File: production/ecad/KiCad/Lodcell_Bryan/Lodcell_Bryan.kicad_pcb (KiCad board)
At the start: 4 copper layers, 50.7 x 23.5 mm, 24 parts, among them J1 LoadCellConnector, J2 power_for_Loadcell, J3 ConnToESP32, U3 ADS1231IDR, U4 TXB0104DR

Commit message: Renamed designators
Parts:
- moved H1 19.6 mm to (170.4, 41.6)
- moved H4 1.21 mm to (190.5, 41.8)
- renumbered C7 to C2, C2 to C3, C3 to C4, C4 to C5, C5 to C6, C6 to C7, R3 to R1, R1 to R3, U3 to U1, U4 to U2
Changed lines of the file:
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@@
 	(net 1 "SPEED")
 	(net 2 "GND")
-	(net 3 "Net-(U3-CAP1)")
-	(net 4 "Net-(U3-CAP2)")
+	(net 3 "Net-(U1-CAP1)")
+	(net 4 "Net-(U1-CAP2)")
 	(net 5 "+5V")
 	(net 6 "+3.3V")
@@
 	(net 13 "/LP_+")
 	(net 14 "/LP_-")
-	(net 15 "Net-(U4-OE)")
-	(net 16 "Net-(U3-~{DRDY}{slash}DOUT)")
-	(net 17 "Net-(U3-~{PDWN})")
-	(net 18 "Net-(U3-SCLK)")
-	(net 19 "Net-(U3-SPEED)")
+	(net 15 "Net-(U2-OE)")
+	(net 16 "Net-(U1-~{DRDY}{slash}DOUT)")
+	(net 17 "Net-(U1-~{PDWN})")
+	(net 18 "Net-(U1-SCLK)")
+	(net 19 "Net-(U1-SPEED)")
 	(footprint "TXB0104DR:SOIC127P600X175-14N"
 		(layer "F.Cu")
 		(at 185.725 64.94)
-		(property "Reference" "U4"
+		(property "Reference" "U2"
 			(at -4.675 -3.19 180)
 			(layer "F.SilkS")
@@
 			(layers "F.Cu" "F.Paste" "F.Mask")
 			(roundrect_rratio 0.25)
-			(net 16 "Net-(U3-~{DRDY}{slash}DOUT)")
+			(net 16 "Net-(U1-~{DRDY}{slash}DOUT)")
 			(pinfunction "A1")
 			(pintype "input")
@@
 			(layers "F.Cu" "F.Paste" "F.Mask")
 			(roundrect_rratio 0.25)
-			(net 18 "Net-(U3-SCLK)")
+			(net 18 "Net-(U1-SCLK)")
 			(pinfunction "A2")
 			(pintype "input")
@@
 			(layers "F.Cu" "F.Paste" "F.Mask")
 			(roundrect_rratio 0.25)
-			(net 17 "Net-(U3-~{PDWN})")
+			(net 17 "Net-(U1-~{PDWN})")
 			(pinfunction "A3")
 			(pintype "input")
@@
 			(layers "F.Cu" "F.Paste" "F.Mask")
 			(roundrect_rratio 0.25)
-			(net 19 "Net-(U3-SPEED)")
+			(net 19 "Net-(U1-SPEED)")
 			(pinfunction "A4")
 			(pintype "input")
@@
 			(layers "F.Cu" "F.Paste" "F.Mask")
 			(roundrect_rratio 0.25)
-			(net 15 "Net-(U4-OE)")
+			(net 15 "Net-(U2-OE)")
 			(pinfunction "OE")
 			(pintype "input")
@@
 		(descr "Resistor SMD 0805 (2012 Metric), square (rectangular) end terminal, IPC_7351 nominal with elongated pad for handsoldering. (Body size source: IPC-SM-782 page 72, https://www.pcb-3d.com/wordpress/wp-content/uploads/ipc-sm-782a_amendment_1_and_2.pdf), generated with kicad-footprint-generator")
 		(tags "resistor handsolder")
-		(property "Reference" "R3"
+		(property "Reference" "R1"
 			(at 2.5716 0.5034 180)
 			(layer "F.SilkS")
@@
 			(size 1.5 1.5)
 			(layers "F.Cu" "F.Mask")
-			(net 16 "Net-(U3-~{DRDY}{slash}DOUT)")
+			(net 16 "Net-(U1-~{DRDY}{slash}DOUT)")
 			(pinfunction "1")
 			(pintype "passive")
@@
 	(footprint "MountingHole:MountingHole_2.5mm"
 		(layer "F.Cu")
-		(at 190.75 40.575)
+		(at 190.475 41.75)
 		(descr "Mounting Hole 2.5mm, no annular")
 		(tags "mounting hole 2.5mm no annular")
@@
 			(layers "F.Cu" "F.Paste" "F.Mask")
 			(roundrect_rratio 0.208333)
-			(net 15 "Net-(U4-OE)")
+			(net 15 "Net-(U2-OE)")
 			(pintype "passive")
 		)
@@
 		(descr "Capacitor SMD 0805 (2012 Metric), square (rectangular) end terminal, IPC_7351 nominal with elongated pad for handsoldering. (Body size source: IPC-SM-782 page 76, https://www.pcb-3d.com/wordpress/wp-content/uploads/ipc-sm-782a_amendment_1_and_2.pdf, https://docs.google.com/spreadsheets/d/1BsfQQcO9C6DZCsRaXUlFlo91Tg2WpOkGARC1WS5S8t0/edit?usp=sharing), generated with kicad-footprint-generator")
 		(tags "capacitor handsolder")
-		(property "Reference" "C2"
+		(property "Reference" "C3"
 			(at -2.5 0.3 180)
 			(layer "F.SilkS")
@@
 			(layers "F.Cu" "F.Paste" "F.Mask")
 			(roundrect_rratio 0.212766)
-			(net 3 "Net-(U3-CAP1)")
+			(net 3 "Net-(U1-CAP1)")
 			(pintype "passive")
 		)
@@
 			(layers "F.Cu" "F.Paste" "F.Mask")
 			(roundrect_rratio 0.212766)
-			(net 4 "Net-(U3-CAP2)")
+			(net 4 "Net-(U1-CAP2)")
 			(pintype "passive")
 		)
@@
 	(footprint "MountingHole:MountingHole_2.5mm"
 		(layer "F.Cu")
-		(at 151.2 38.125)
+		(at 170.45 41.575)
 		(descr "Mounting Hole 2.5mm, no annular")
 		(tags "mounting hole 2.5mm no annular")
@@
 		(descr "Capacitor SMD 0805 (2012 Metric), square (rectangular) end terminal, IPC_7351 nominal with elongated pad for handsoldering. (Body size source: IPC-SM-782 page 76, https://www.pcb-3d.com/wordpress/wp-content/uploads/ipc-sm-782a_amendment_1_and_2.pdf, https://docs.google.com/spreadsheets/d/1BsfQQcO9C6DZCsRaXUlFlo91Tg2WpOkGARC1WS5S8t0/edit?usp=sharing), generated with kicad-footprint-generator")
 		(tags "capacitor handsolder")
-		(property "Reference" "C5"
+		(property "Reference" "C6"
 			(at -2.5 0.25 180)
 			(layer "F.SilkS")
@@
 		(descr "Capacitor SMD 0805 (2012 Metric), square (rectangular) end terminal, IPC_7351 nominal with elongated pad for handsoldering. (Body size source: IPC-SM-782 page 76, https://www.pcb-3d.com/wordpress/wp-content/uploads/ipc-sm-782a_amendment_1_and_2.pdf, https://docs.google.com/spreadsheets/d/1BsfQQcO9C6DZCsRaXUlFlo91Tg2WpOkGARC1WS5S8t0/edit?usp=sharing), generated with kicad-footprint-generator")
 		(tags "capacitor handsolder")
-		(property "Reference" "C6"
+		(property "Reference" "C7"
 			(at -2.45 0.1 0)
 			(layer "F.SilkS")
@@
 		(descr "Resistor SMD 0805 (2012 Metric), square (rectangular) end terminal, IPC_7351 nominal with elongated pad for handsoldering. (Body size source: IPC-SM-782 page 72, https://www.pcb-3d.com/wordpress/wp-content/uploads/ipc-sm-782a_amendment_1_and_2.pdf), generated with kicad-footprint-generator")
 		(tags "resistor handsolder")
-		(property "Reference" "R1"
+		(property "Reference" "R3"
 			(at 2.5466 0.4784 180)
 			(layer "F.SilkS")
@@
 		(descr "Capacitor SMD 0805 (2012 Metric), square (rectangular) end terminal, IPC_7351 nominal with elongated pad for handsoldering. (Body size source: IPC-SM-782 page 76, https://www.pcb-3d.com/wordpress/wp-content/uploads/ipc-sm-782a_amendment_1_and_2.pdf, https://docs.google.com/spreadsheets/d/1BsfQQcO9C6DZCsRaXUlFlo91Tg2WpOkGARC1WS5S8t0/edit?usp=sharing), generated with kicad-footprint-generator")
 		(tags "capacitor handsolder")
-		(property "Reference" "C3"
+		(property "Reference" "C4"
 			(at 1.05 1.7 180)
 			(layer "F.SilkS")
@@
 		(layer "F.Cu")
 		(at 171.8 66.9)
-		(property "Reference" "U3"
+		(property "Reference" "U1"
 			(at -4.75 -4 0)
 			(layer "F.SilkS")
@@
 			(layers "F.Cu" "F.Paste" "F.Mask")
 			(roundrect_rratio 0.125)
-			(net 19 "Net-(U3-SPEED)")
+			(net 19 "Net-(U1-SPEED)")
 			(pinfunction "SPEED")
 			(pintype "input")
@@
 			(layers "F.Cu" "F.Paste" "F.Mask")
 			(roundrect_rratio 0.125)
-			(net 3 "Net-(U3-CAP1)")
+			(net 3 "Net-(U1-CAP1)")
 			(pinfunction "CAP1")
 			(pintype "passive")
@@
 			(layers "F.Cu" "F.Paste" "F.Mask")
 			(roundrect_rratio 0.125)
-			(net 4 "Net-(U3-CAP2)")
+			(net 4 "Net-(U1-CAP2)")
 			(pinfunction "CAP2")
 			(pintype "passive")
@@
 			(layers "F.Cu" "F.Paste" "F.Mask")
 			(roundrect_rratio 0.125)
-			(net 17 "Net-(U3-~{PDWN})")
+			(net 17 "Net-(U1-~{PDWN})")
 			(pinfunction "~{PDWN}")
 			(pintype "input")
@@
 			(layers "F.Cu" "F.Paste" "F.Mask")
 			(roundrect_rratio 0.125)
-			(net 18 "Net-(U3-SCLK)")
+			(net 18 "Net-(U1-SCLK)")
 			(pinfunction "SCLK")
 			(pintype "input")
@@
 			(layers "F.Cu" "F.Paste" "F.Mask")
 			(roundrect_rratio 0.125)
-			(net 16 "Net-(U3-~{DRDY}{slash}DOUT)")
+			(net 16 "Net-(U1-~{DRDY}{slash}DOUT)")
 			(pinfunction "~{DRDY}/DOUT")
 			(pintype "output")
@@
 			(layers "F.Cu" "F.Paste" "F.Mask")
 			(roundrect_rratio 0.208333)
-			(net 15 "Net-(U4-OE)")
+			(net 15 "Net-(U2-OE)")
 			(pintype "passive")
 		)
@@
 		(descr "Capacitor SMD 0805 (2012 Metric), square (rectangular) end terminal, IPC_7351 nominal with elongated pad for handsoldering. (Body size source: IPC-SM-782 page 76, https://www.pcb-3d.com/wordpress/wp-content/uploads/ipc-sm-782a_amendment_1_and_2.pdf, https://docs.google.com/spreadsheets/d/1BsfQQcO9C6DZCsRaXUlFlo91Tg2WpOkGARC1WS5S8t0/edit?usp=sharing), generated with kicad-footprint-generator")
 		(tags "capacitor handsolder")
-		(property "Reference" "C7"
+		(property "Reference" "C2"
 			(at -0.9909 -1.6466 0)
 			(layer "F.SilkS")
@@
 		(descr "Capacitor SMD 0805 (2012 Metric), square (rectangular) end terminal, IPC_7351 nominal with elongated pad for handsoldering. (Body size source: IPC-SM-782 page 76, https://www.pcb-3d.com/wordpress/wp-content/uploads/ipc-sm-782a_amendment_1_and_2.pdf, https://docs.google.com/spreadsheets/d/1BsfQQcO9C6DZCsRaXUlFlo91Tg2WpOkGARC1WS5S8t0/edit?usp=sharing), generated with kicad-footprint-generator")
 		(tags "capacitor handsolder")
-		(property "Reference" "C4"
+		(property "Reference" "C5"
 			(at -2.55 -0.05 0)
 			(layer "F.SilkS")
@@
 	)
 	(segment
-		(start 164.1466 69.3966)
-		(end 165.225 70.475)
-		(width 0.2)
-		(layer "F.Cu")
-		(net 13)
-	)
-	(segment
-		(start 165.225 70.475)
-		(end 166.2 70.475)
+		(start 164.1466 62.1716)
+		(end 164.1466 69.1216)
 		(width 0.2)
 		(layer "F.Cu")
@@
 	)
 	(segment
-		(start 164.1466 62.1716)
-		(end 164.1466 69.3966)
+		(start 162.8534 60.8784)
+		(end 164.1466 62.1716)
 		(width 0.2)
 		(layer "F.Cu")
@@
 	)
 	(segment
-		(start 162.8534 60.8784)
-		(end 164.1466 62.1716)
+		(start 158.2216 60.8784)
+		(end 162.8534 60.8784)
 		(width 0.2)
 		(layer "F.Cu")
@@
 	)
 	(segment
-		(start 158.2216 60.8784)
-		(end 162.8534 60.8784)
+		(start 164.1466 69.1216)
+		(end 165.5 70.475)
 		(width 0.2)
 		(layer "F.Cu")
@@
 		(width 0.2)
 		(layer "F.Cu")
+		(net 13)
+	)
+	(segment
+		(start 165.5 70.475)
+		(end 166.2 70.475)
+		(width 0.2)
+		(layer "F.Cu")

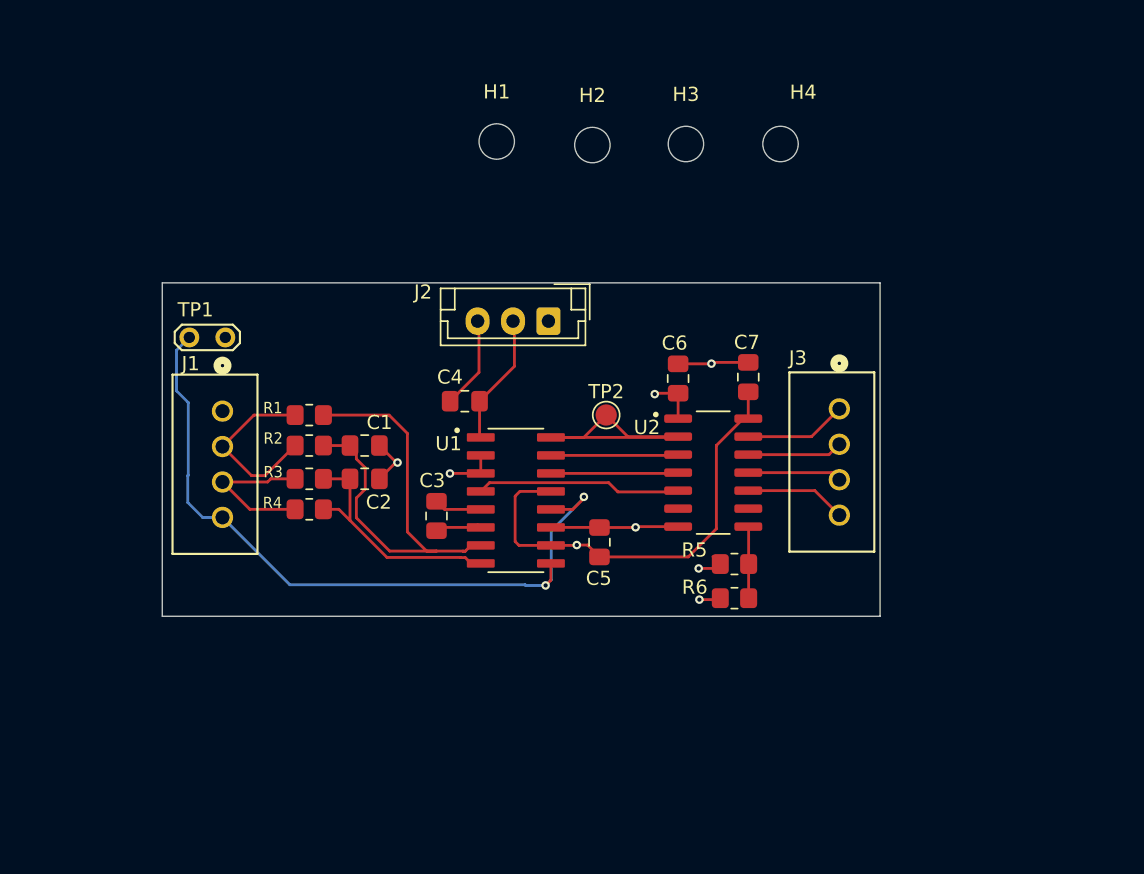
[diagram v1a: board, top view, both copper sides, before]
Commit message: Improved differential signals. switched to 2 layer board
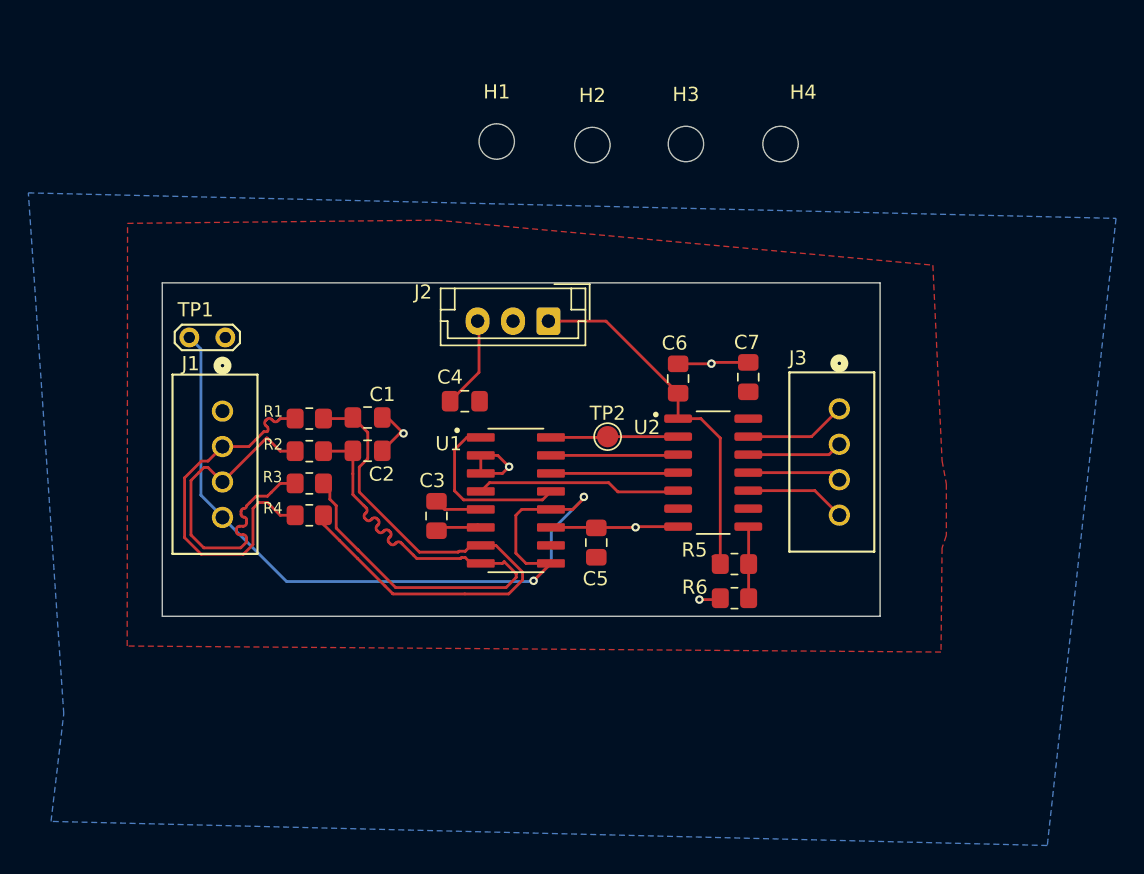
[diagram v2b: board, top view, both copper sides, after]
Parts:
- moved R4 7.07 mm to (157.2, 68.0)
- moved C1 1.99 mm to (161.3, 61.0)
- moved C2 1.99 mm to (161.3, 63.4)
- moved R2 1.95 mm to (157.2, 63.4)
- moved R1 1.90 mm to (157.2, 61.1)
- moved R3 1.83 mm to (157.2, 65.7)
- moved TP2 1.53 mm to (178.3, 62.4)
- moved C5 0.23 mm to (177.5, 69.9)
- renumbered R2 to R1, R3 to R2, R4 to R3, R1 to R4
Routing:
- net +5V: track 40.4 -> 12.9 mm, vias 1 -> 0
- net /LP_-: track 17.5 -> 39.9 mm
- net +3.3V: track 6.37 -> 27.2 mm, vias 2 -> 0
- net /RawLoadCell_-: track 11.1 -> 26.2 mm
- net /RawLoadCell_+: track 12.9 -> 26.2 mm
- net Net-(U1-~{DRDY}/DOUT): track 19.3 -> 9.08 mm
- net /LP_+: track 33.6 -> 40.9 mm
- net Net-(J1-Pin_4): track 52.2 -> 58.0 mm
- net GND: track 29.0 -> 30.8 mm
- added copper zone on F.Cu, net +5V
- added copper zone on B.Cu, net GND
- removed copper zone on In1.Cu, net +3.3V
- removed copper zone on In1.Cu, net +5V
- removed copper zone on In2.Cu, net GND

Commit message: added holes
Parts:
- removed H1: UpperLeftMH, MountingHole:MountingHole_2.5mm
- removed H2: UpperRightMH, MountingHole:MountingHole_2.5mm
- removed H3: BottomLeftMH, MountingHole:MountingHole_2.5mm
- removed H4: LowerRightMH, MountingHole:MountingHole_2.5mm
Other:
- board size 50.7 x 23.5 mm -> 59.2 x 31 mm

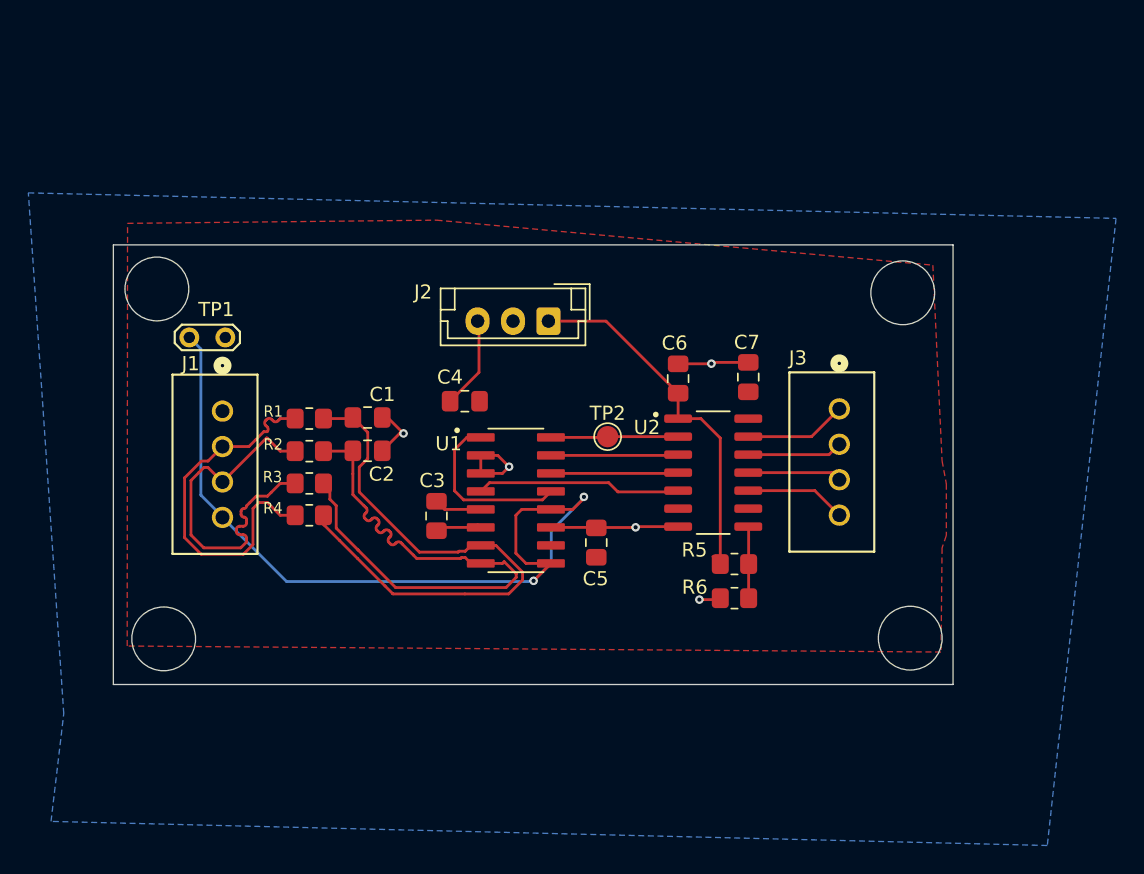
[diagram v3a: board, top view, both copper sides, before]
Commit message: Added more clearance for mounting holes
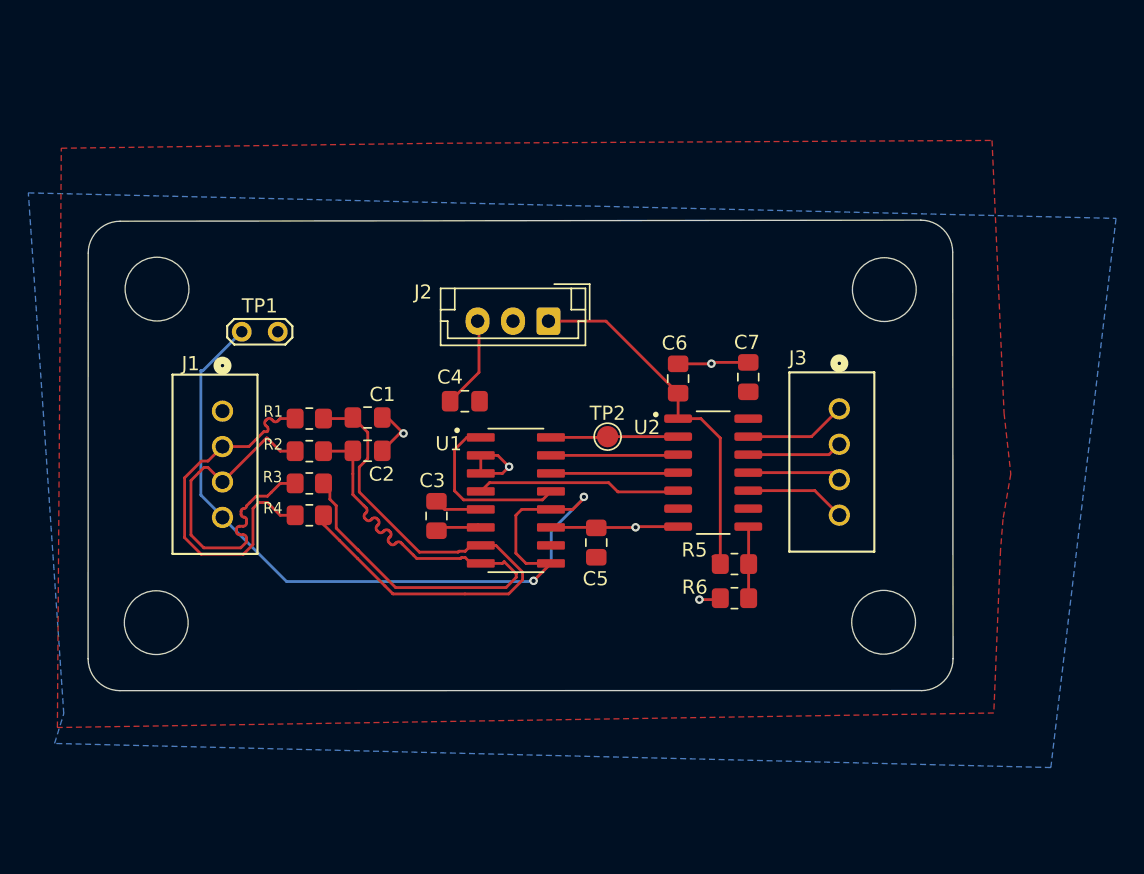
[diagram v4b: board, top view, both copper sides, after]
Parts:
- added ?: LOGO, LOGO, B.Cu at (172.7, 64.2)
- added G***: LOGO, LOGO, B.Cu at (159.5, 64.0)
- added G***: LOGO, LOGO, B.Cu at (186.2, 64.0)
- added H1: UpperLeftMH, MountingHole:MountingHole_4.5mm, F.Cu at (146.5, 52.0)
- added H2: UpperRightMH, MountingHole:MountingHole_4.5mm, F.Cu at (197.8, 52.0)
- added H3: BottomLeftMH, MountingHole:MountingHole_4.5mm, F.Cu at (146.4, 75.5)
- added H4: LowerRightMH, MountingHole:MountingHole_4.5mm, F.Cu at (197.8, 75.5)
- moved TP1 3.72 mm to (155.0, 55.0)
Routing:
- net Net-(J1-Pin_4): track 58.0 -> 59.3 mm
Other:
- board size 59.2 x 31 mm -> 61 x 33.2 mm
- copper layers 4 -> 2
- board text added: "Designed by Bryan Pitts"
